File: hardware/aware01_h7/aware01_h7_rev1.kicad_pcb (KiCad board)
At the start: 4 copper layers, 76.7 x 110 mm, 138 parts, among them IC2 TLV320AIC3204IRHBR, J1 Conn_01x06_Pin, J10 CV1_IN, J11 InL, J13 OutR, J2 Conn_01x03_Pin, J3 Conn_02x05_Odd_Even, J4 InR, J5 GATE1_IN, J6 OutL, J7 GATE2_IN, J8 CV2_IN, J9 V/OCT_IN, Q1 MMBT3904, Q2 MMBT3904, SW1 SW_Push, SW2 SW_Push, SW3 SW_Push, U1 STM32H7B0ZBTx, U10 NE5532DRG4, U11 LMV722IDR, U13 LMV722IDR, U2 IS45S16800F-7TLA2, U3 10k, U4 10k, U5 10k, U6 10k, U7 LM1117MP-3.3, U8 LM4040DBZ-10, U9 NE5532DRG4, Y1 WE-XTAL 24.0MHz 50ppm

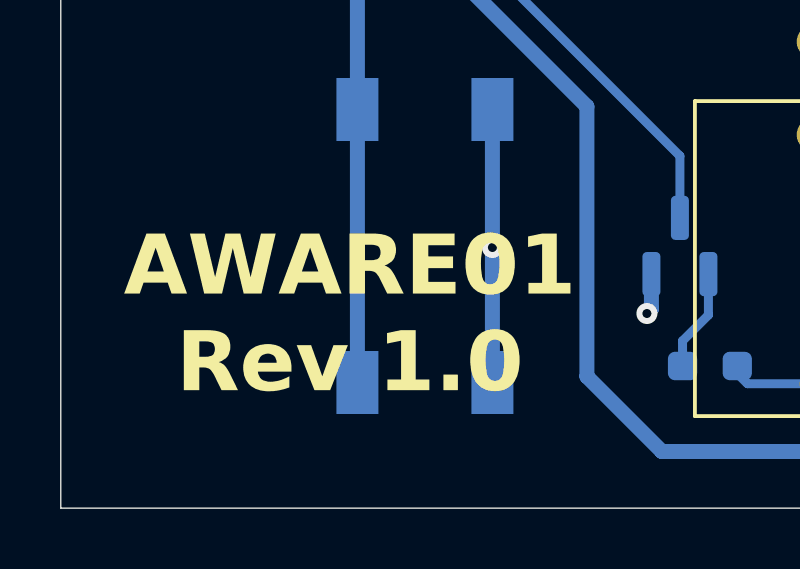
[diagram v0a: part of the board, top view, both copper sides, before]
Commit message: change PWR to GND plane and reroute 3V3
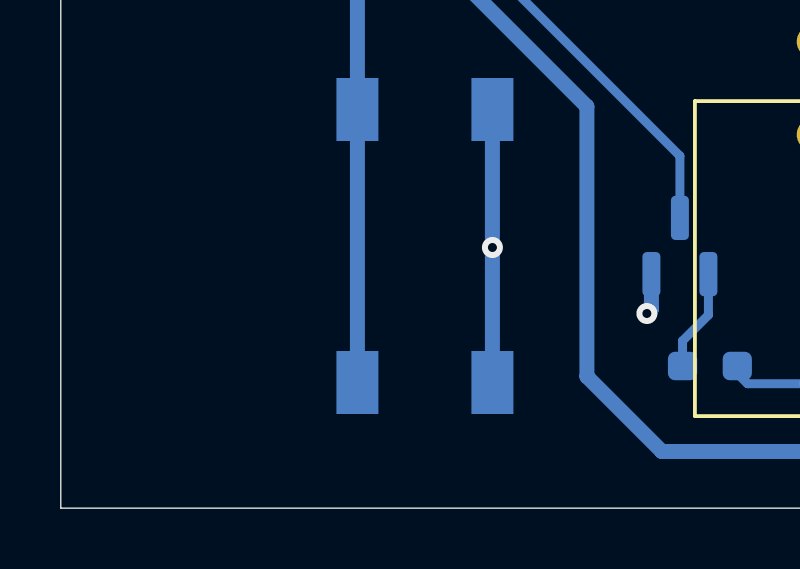
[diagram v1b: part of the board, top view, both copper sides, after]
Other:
- board text removed: "AWARE01 Rev 1.0"
